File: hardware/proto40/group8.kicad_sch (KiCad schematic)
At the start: 36 parts, among them U1101 TMUX1308, U1102 74HC165

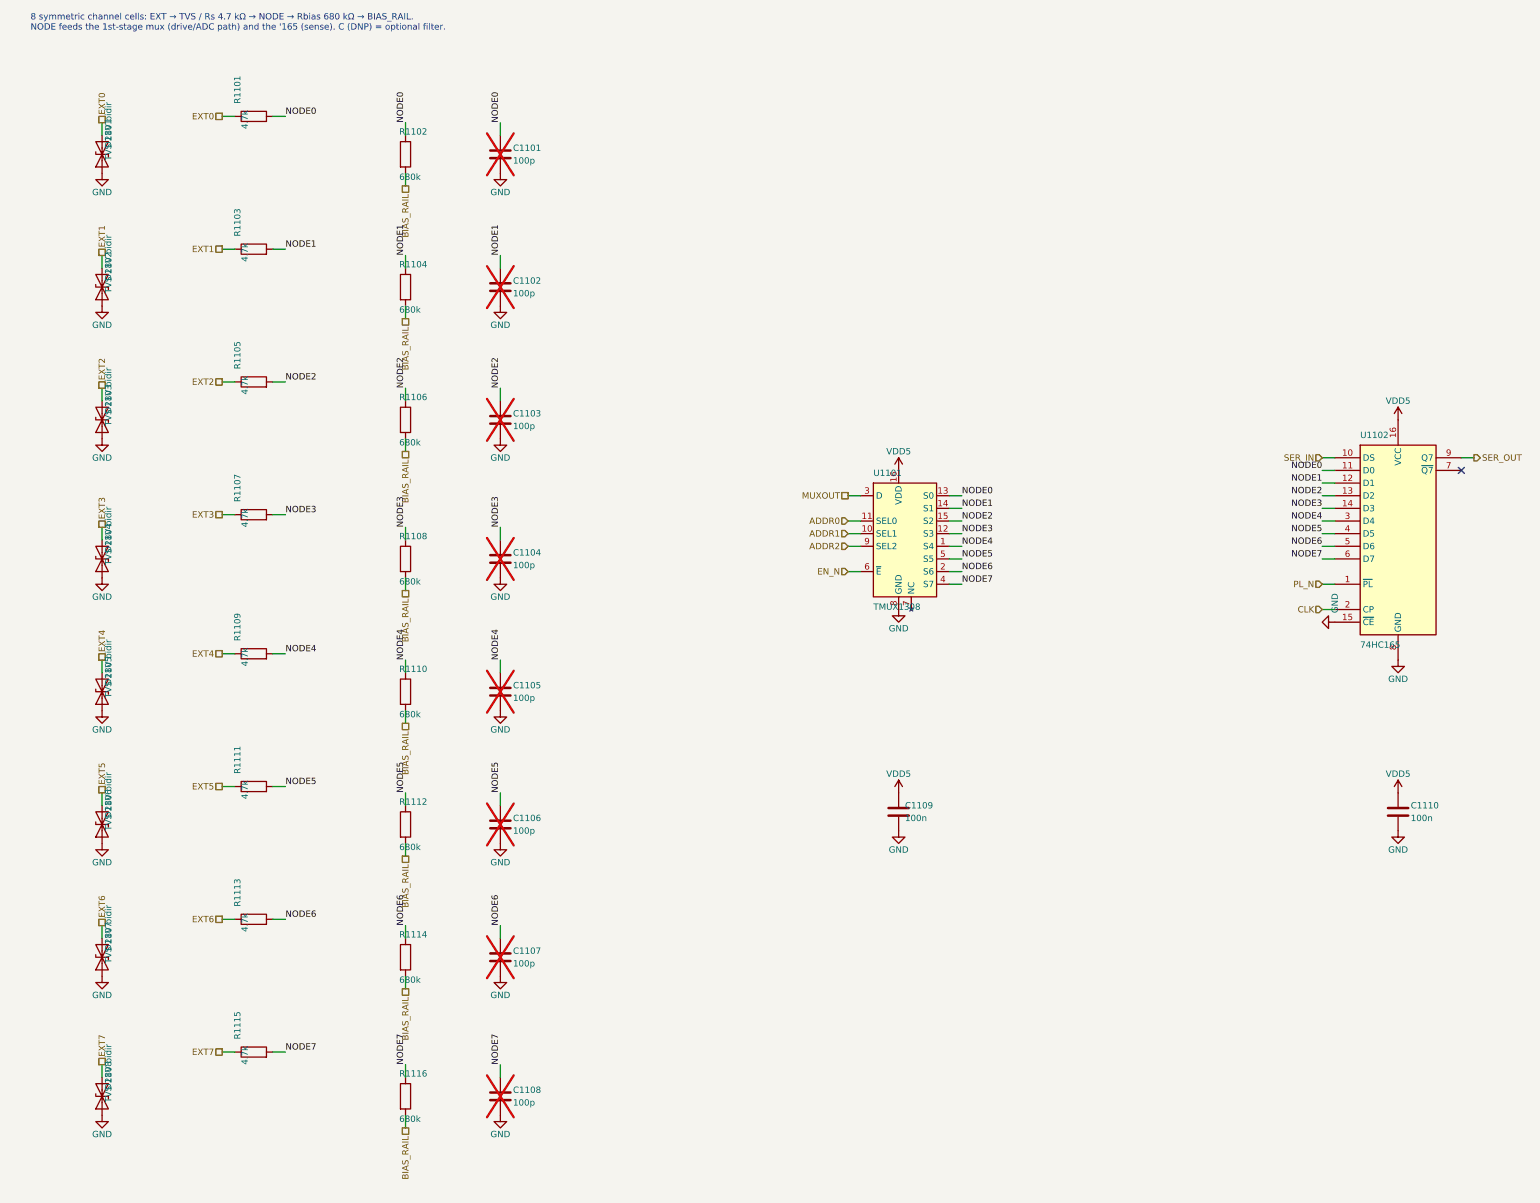
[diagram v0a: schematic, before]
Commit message: Redraw Proto40 schematic with wired functional blocks
Review feedback: text overlapped components and parts were isolated
islands joined only by labels, so connectivity was hard to follow.

- Generator: polyline wires, automatic junctions, text placement from
  the real symbol body graphics, KiCad field-angle handling for rotated
  symbols, power symbols oriented normally on horizontal pins
- Sheets redrawn left-to-right with wired blocks: channel cells, BIAS
  rail, decoupling on IC power pins, pull-ups on their lines, control
  ladder across the six groups, visible 165 chain, wired root hierarchy
  (MCU -> Control -> both sides) and cross-side LOOP
- layoutcheck.py: rejects text/text, text/body, text/wire overlaps and
  wires through bodies; CI runs the generator with --strict
- check_proto40.py: finds parts by sheet path and follows pins, so it no
  longer depends on net names or reference numbering

ERC 0 violations, design-intent audit PASS, layout issues 0.

Co-Authored-By: Claude Opus 5.5 <noreply@anthropic.com>
Claude-Session: https://claude.ai/code/session_01UG7pR5ZtgvoVGRWFojzQKf
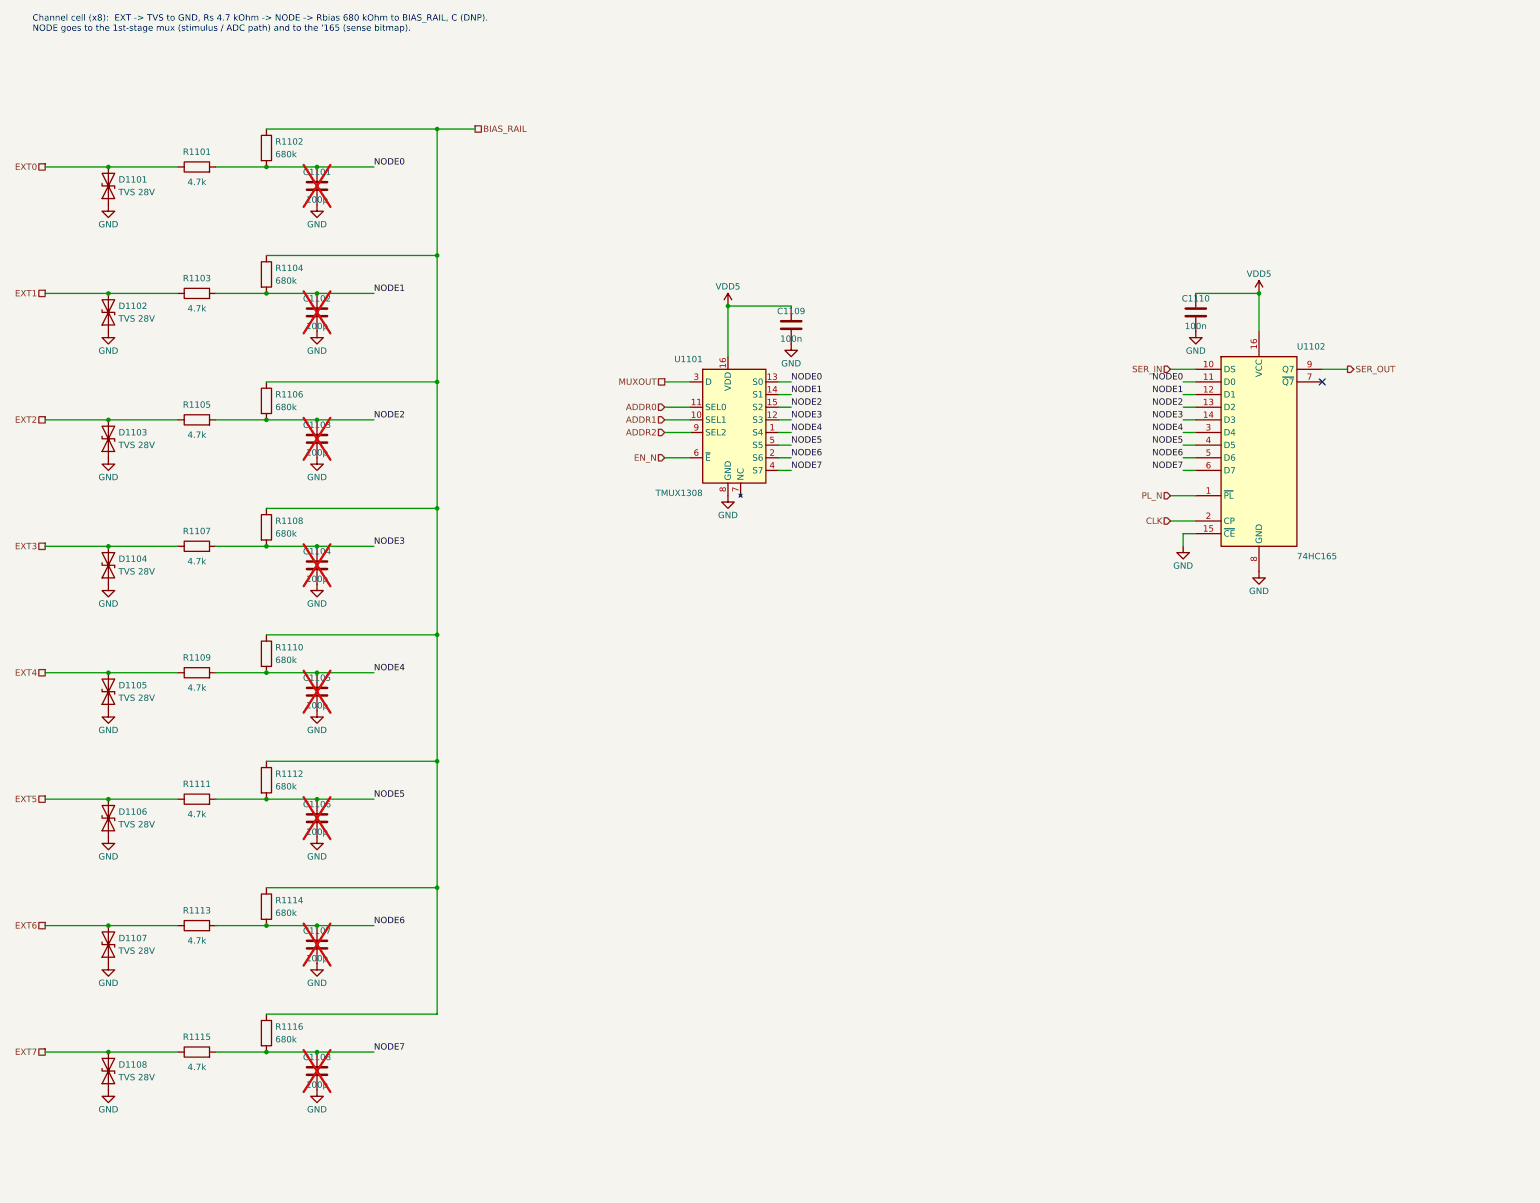
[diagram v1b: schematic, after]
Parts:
- D1101, D1102, D1103, D1104, D1105, D1106, D1107, D1108: value TVS 28V bidir -> TVS 28V
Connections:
- net BIAS_RAIL: now also R1102.1, R1104.1, R1106.1, R1108.1, R1110.1, R1112.1, R1114.1, R1116.1; no longer R1102.2, R1104.2, R1106.2, R1108.2, R1110.2, R1112.2, R1114.2, R1116.2
- net NODE0: now also R1102.2; no longer R1102.1
- net NODE1: now also R1104.2; no longer R1104.1
- net NODE2: now also R1106.2; no longer R1106.1
- net NODE3: now also R1108.2; no longer R1108.1
- net NODE4: now also R1110.2; no longer R1110.1
- net NODE5: now also R1112.2; no longer R1112.1
- net NODE6: now also R1114.2; no longer R1114.1
- net NODE7: now also R1116.2; no longer R1116.1
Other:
- note added: "Channel cell (x8): EXT -> TVS to GND, Rs 4.7 kOhm -> NODE -> Rbias 680 kOhm to BIAS_RAIL, C (DNP). NODE goes to the 1st-stage mux (stimulus / ADC path) and to the '165 (sense bitmap)."
- note removed: "8 symmetric channel cells: EXT → TVS / Rs 4.7 kΩ → NODE → Rbias 680 kΩ → BIAS_RAIL. NODE feeds the 1st-stage mux (drive/ADC path) and the '165 (sense). C (DNP) = optional filter."
- moved on the sheet: C1101, C1102, C1103, C1104, C1105, C1106, C1107, C1108, C1109, C1110, D1101, D1102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
